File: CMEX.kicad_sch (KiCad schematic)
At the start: 0 parts

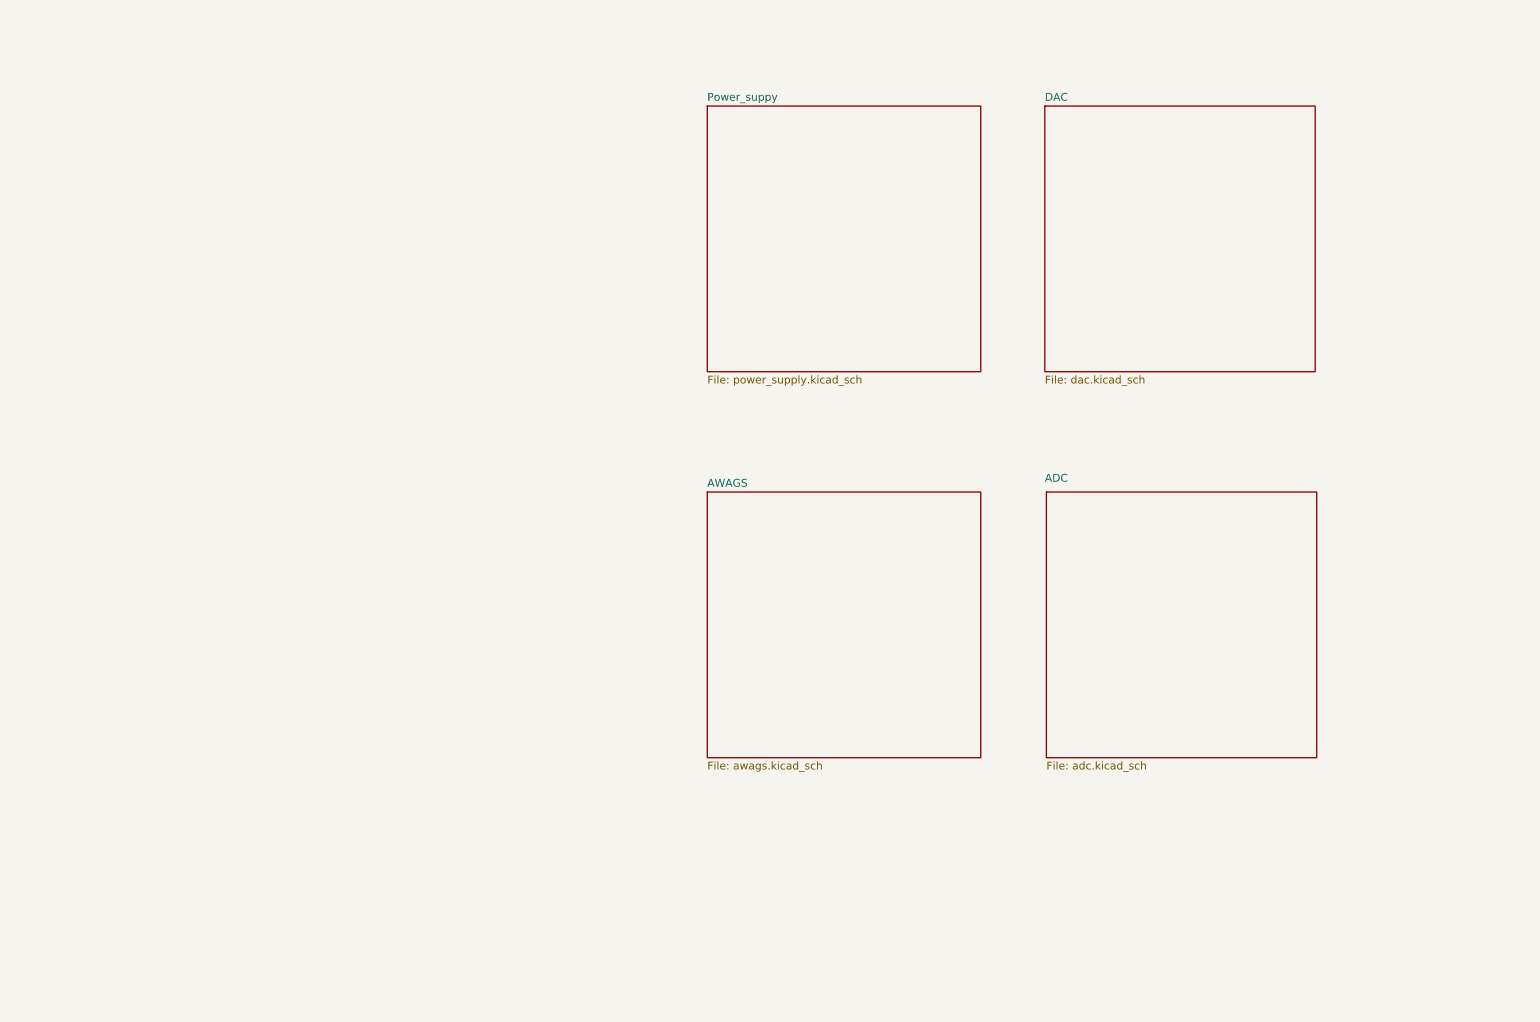
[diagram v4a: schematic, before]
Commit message: Changed global to hierarchichal lables, reorganized main sheet to get pins to connector.
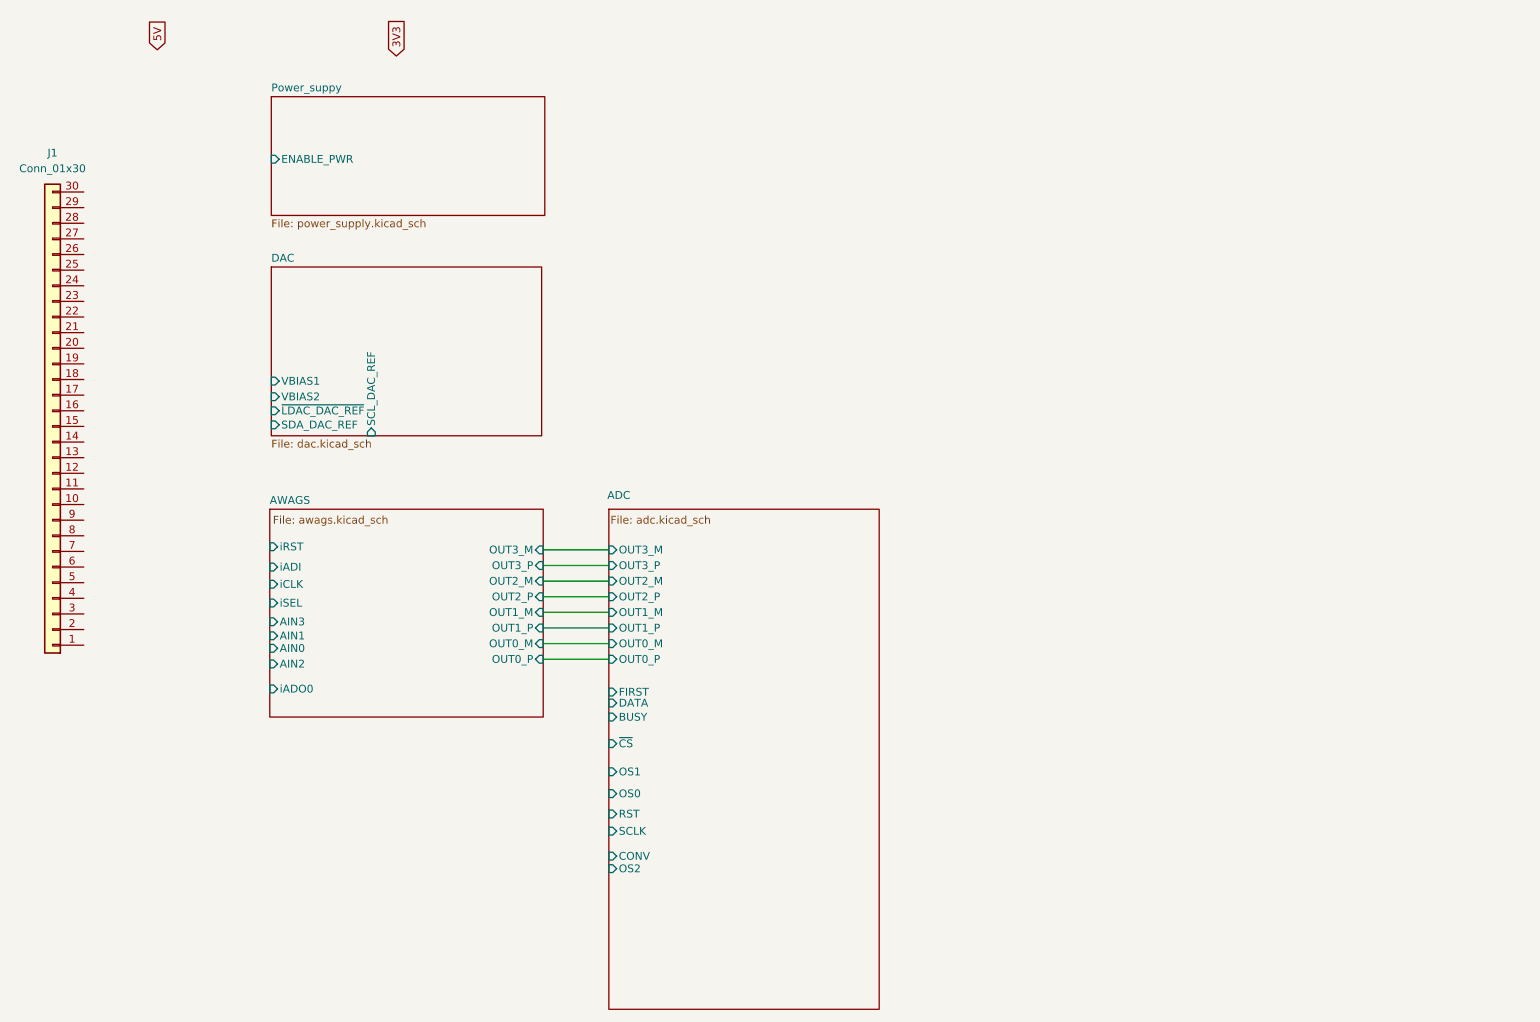
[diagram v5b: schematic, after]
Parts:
- added J1: Conn_01x30, symbol Connector_Generic:Conn_01x30
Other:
- sheet ADC ports: added BUSY, CONV, DATA, FIRST, OS0, OS1, OS2, OUT0_M, OUT0_P, OUT1_M, OUT1_P, OUT2_M, OUT2_P, OUT3_M, OUT3_P, RST, SCLK, ~{CS}; removed none
- sheet AWAGS ports: added AIN0, AIN1, AIN2, AIN3, OUT0_M, OUT0_P, OUT1_M, OUT1_P, OUT2_M, OUT2_P, OUT3_M, OUT3_P, iADI, iADO0, iCLK, iRST, iSEL; removed none
- sheet DAC ports: added SCL_DAC_REF, SDA_DAC_REF, VBIAS1, VBIAS2, ~{LDAC_DAC_REF}; removed none
- sheet Power_suppy ports: added ENABLE_PWR; removed none

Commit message: Added connector to all sheets.
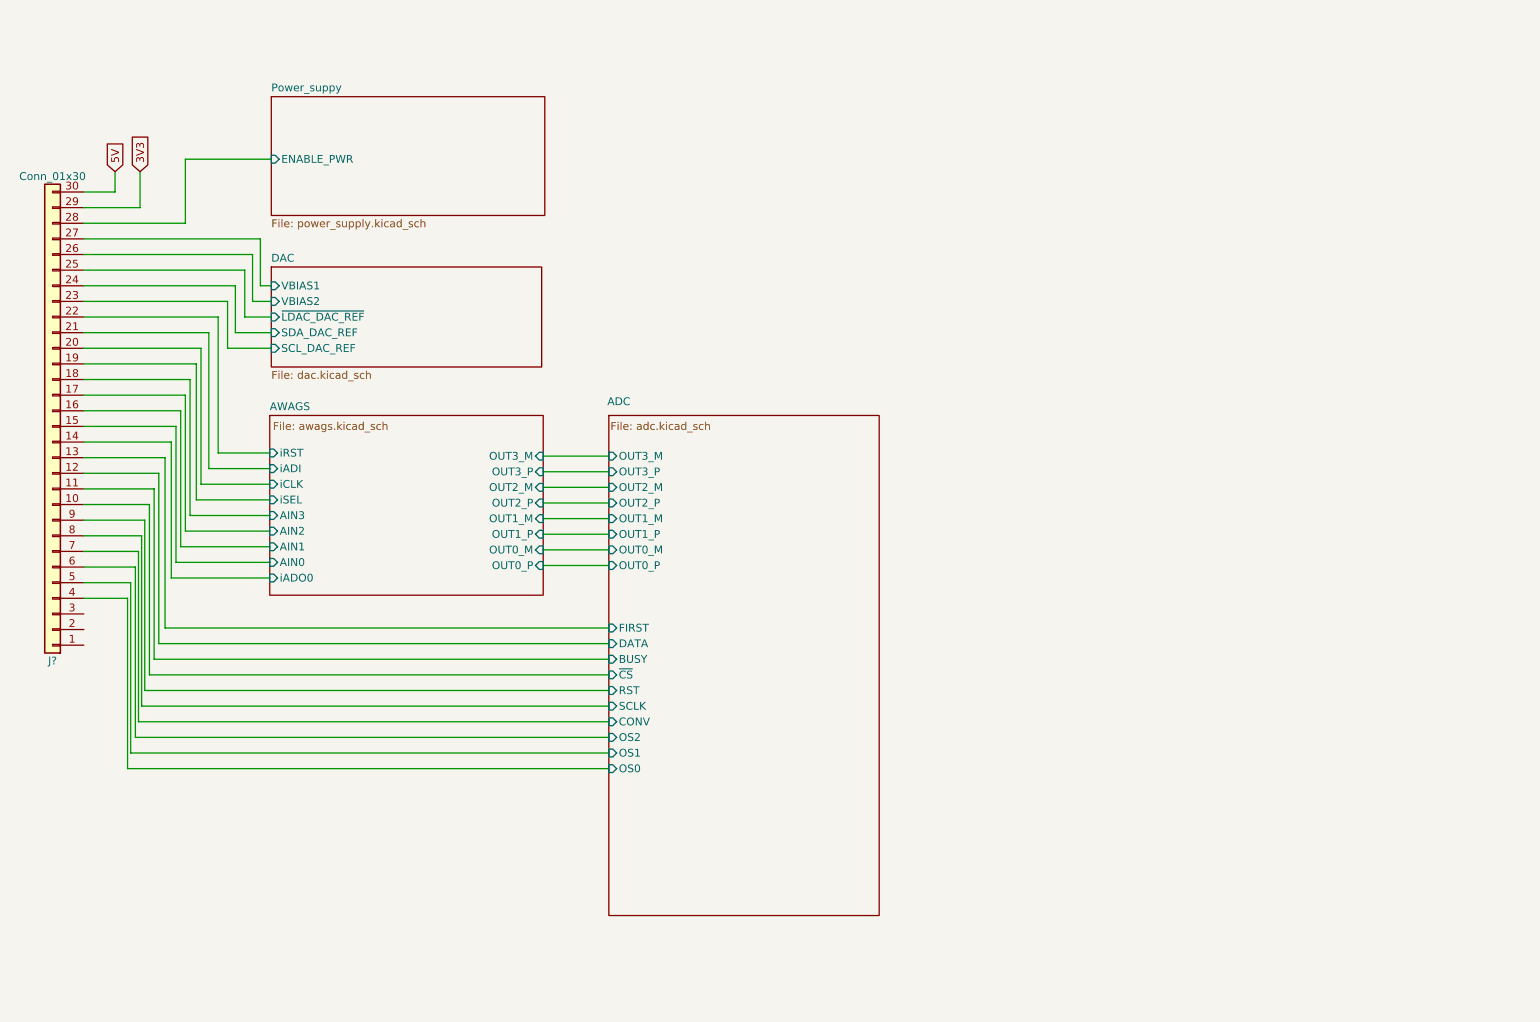
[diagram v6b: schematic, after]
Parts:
- J?: renamed from J1; footprint (none) -> Connector_PinHeader_1.27mm:PinHeader_1x30_P1.27mm_Vertical
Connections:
- net 3V3: now also J?.29 (Pin_29)
- net 5V: now also J?.30 (Pin_30)
- net ADC/BUSY: now also J?.11 (Pin_11)
- net ADC/CONV: now also J?.7 (Pin_7)
- net ADC/DATA: now also J?.12 (Pin_12)
- net ADC/FIRST: now also J?.13 (Pin_13)
- net ADC/OS0: now also J?.4 (Pin_4)
- net ADC/OS1: now also J?.5 (Pin_5)
- net ADC/OS2: now also J?.6 (Pin_6)
- net ADC/RST: now also J?.9 (Pin_9)
- net ADC/SCLK: now also J?.8 (Pin_8)
- net ADC/~{CS}: now also J?.10 (Pin_10)
- net AWAGS/AIN0: now also J?.15 (Pin_15)
- net AWAGS/AIN1: now also J?.16 (Pin_16)
- net AWAGS/AIN2: now also J?.17 (Pin_17)
- net AWAGS/AIN3: now also J?.18 (Pin_18)
- net AWAGS/iADI: now also J?.21 (Pin_21)
- net AWAGS/iADO0: now also J?.14 (Pin_14)
- net AWAGS/iCLK: now also J?.20 (Pin_20)
- net AWAGS/iRST: now also J?.22 (Pin_22)
- net AWAGS/iSEL: now also J?.19 (Pin_19)
- net DAC/SCL_DAC_REF: now also J?.23 (Pin_23)
- net DAC/SDA_DAC_REF: now also J?.24 (Pin_24)
- net DAC/VBIAS1: now also J?.27 (Pin_27)
- net DAC/VBIAS2: now also J?.26 (Pin_26)
- net DAC/~{LDAC_DAC_REF}: now also J?.25 (Pin_25)
- net Power_suppy/ENABLE_PWR: now also J?.28 (Pin_28)

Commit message: Schematic finished, ready for review.
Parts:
- J1: renamed from J?; footprint Connector_PinHeader_1.27mm:PinHeader_1x30_P1.27mm_Vertical -> (none)
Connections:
- net GND: now reaches J1.3 (Pin_3)
- no-connect marks 0 -> 2
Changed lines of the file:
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@@
 (kicad_sch (version 20230121) (generator eeschema)
   (paper "A4")
+  (junction (at 55.118 58.42) (diameter 0) (color 0 0 0 0)
+  )
+  (junction (at 48.768 131.572) (diameter 0) (color 0 0 0 0)
+  )
+  (junction (at 48.514 55.88) (diameter 0) (color 0 0 0 0)
+  )
+  (no_connect (at 45.974 129.54))
+  (no_connect (at 45.974 127))
   (wire (pts (xy 76.454 73.66) (xy 73.406 73.66))
     (stroke (width 0) (type default))
@@
     (stroke (width 0) (type default))
   )
-  (wire (pts (xy 45.974 55.88) (xy 51.054 55.88))
+  (wire (pts (xy 45.974 55.88) (xy 48.514 55.88))
     (stroke (width 0) (type default))
   )
@@
     (stroke (width 0) (type default))
   )
+  (wire (pts (xy 45.974 124.46) (xy 48.768 124.46))
+    (stroke (width 0) (type default))
+  )
   (wire (pts (xy 74.676 71.12) (xy 76.454 71.12))
     (stroke (width 0) (type default))
@@
     (stroke (width 0) (type default))
   )
+  (wire (pts (xy 48.768 124.46) (xy 48.768 131.572))
+    (stroke (width 0) (type default))
+  )
   (wire (pts (xy 120.65 101.346) (xy 131.318 101.346))
     (stroke (width 0) (type default))
@@
     (stroke (width 0) (type default))
   )
+  (wire (pts (xy 48.768 131.572) (xy 48.768 135.636))
+    (stroke (width 0) (type default))
+  )
   (wire (pts (xy 63.246 108.458) (xy 63.246 86.36))
     (stroke (width 0) (type default))
@@
   )
   (wire (pts (xy 45.974 68.58) (xy 72.136 68.58))
+    (stroke (width 0) (type default))
+  )
+  (wire (pts (xy 48.514 55.88) (xy 51.054 55.88))
     (stroke (width 0) (type default))
   )
@@
     )
   )
+  (symbol (lib_id "power:GND") (at 48.768 135.636 0) (unit 1)
+    (in_bom yes) (on_board yes) (dnp no) (fields_autoplaced)
+    (property "Reference" "#PWR01" (at 48.768 141.986 0)
+      (effects (font (size 1.27 1.27)) hide)
+    )
+    (property "Value" "GND" (at 48.768 139.446 0)
+      (effects (font (size 1.27 1.27)))
+    )
+    (property "Footprint" "" (at 48.768 135.636 0)
+      (effects (font (size 1.27 1.27)) hide)
+    )
+    (property "Datasheet" "" (at 48.768 135.636 0)
+      (effects (font (size 1.27 1.27)) hide)
+    )
+    (pin "1")
+    (instances
+      (project "CMEX"
+        (path "/03c4a148-37f4-4d5a-ada3-efb0d725ba7b"
+          (reference "#PWR01") (unit 1)
+        )
+      )
+    )
+  )
+  (symbol (lib_id "power:PWR_FLAG") (at 55.118 58.42 270) (unit 1)
+    (in_bom yes) (on_board yes) (dnp no)
+    (property "Reference" "#FLG03" (at 57.023 58.42 0)
+      (effects (font (size 1.27 1.27)) hide)
+    )
+    (property "Value" "PWR_FLAG" (at 58.928 58.42 0)
+      (effects (font (size 1.27 1.27)))
+    )
+    (property "Footprint" "" (at 55.118 58.42 0)
+      (effects (font (size 1.27 1.27)) hide)
+    )
+    (property "Datasheet" "~" (at 55.118 58.42 0)
+      (effects (font (size 1.27 1.27)) hide)
+    )
+    (pin "1")
+    (instances
+      (project "CMEX"
+        (path "/03c4a148-37f4-4d5a-ada3-efb0d725ba7b"
+          (reference "#FLG03") (unit 1)
+        )
+      )
+    )
+  )
+  (symbol (lib_id "power:PWR_FLAG") (at 48.514 55.88 0) (unit 1)
+    (in_bom yes) (on_board yes) (dnp no)
+    (property "Reference" "#FLG01" (at 48.514 53.975 0)
+      (effects (font (size 1.27 1.27)) hide)
+    )
+    (property "Value" "PWR_FLAG" (at 48.514 52.07 0)
+      (effects (font (size 1.27 1.27)))
+    )
+    (property "Footprint" "" (at 48.514 55.88 0)
+      (effects (font (size 1.27 1.27)) hide)
+    )
+    (property "Datasheet" "~" (at 48.514 55.88 0)
+      (effects (font (size 1.27 1.27)) hide)
+    )
+    (pin "1")
+    (instances
+      (project "CMEX"
+        (path "/03c4a148-37f4-4d5a-ada3-efb0d725ba7b"
+          (reference "#FLG01") (unit 1)
+        )
+      )
+    )
+  )
   (symbol (lib_id "Connector_Generic:Conn_01x30") (at 40.894 93.98 180) (unit 1)
     (in_bom yes) (on_board yes) (dnp no) (fields_autoplaced)
-    (property "Reference" "J?" (at 40.894 132.08 0)
+    (property "Reference" "J1" (at 40.894 132.08 0)
       (effects (font (size 1.27 1.27)))
     )
@@
       (effects (font (size 1.27 1.27)))
     )
-    (property "Footprint" "Connector_PinHeader_1.27mm:PinHeader_1x30_P1.27mm_Vertical" (at 40.894 93.98 0)
+    (property "Footprint" "" (at 40.894 93.98 0)
       (effects (font (size 1.27 1.27)) hide)
     )
@@
       (project "CMEX"
         (path "/03c4a148-37f4-4d5a-ada3-efb0d725ba7b"
-          (reference "J?") (unit 1)
+          (reference "J1") (unit 1)
         )
       )
+    )
+  )
+  (symbol (lib_id "power:PWR_FLAG") (at 48.768 131.572 270) (unit 1)
+    (in_bom yes) (on_board yes) (dnp no)
+    (property "Reference" "#FLG02" (at 50.673 131.572 0)
+      (effects (font (size 1.27 1.27)) hide)
+    )
+    (property "Value" "PWR_FLAG" (at 52.578 131.572 0)
+      (effects (font (size 1.27 1.27)))
+    )
+    (property "Footprint" "" (at 48.768 131.572 0)
+      (effects (font (size 1.27 1.27)) hide)
+    )
+    (property "Datasheet" "~" (at 48.768 131.572 0)
+      (effects (font (size 1.27 1.27)) hide)
+    )
+    (pin "1")
+    (instances
+      (project "CMEX"
+        (path "/03c4a148-37f4-4d5a-ada3-efb0d725ba7b"
+          (reference "#FLG02") (unit 1)
+        )
+      )

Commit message: Layout erster Entwurf fertig.
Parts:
- J1: footprint (none) -> Connector_PinHeader_1.27mm:PinHeader_1x30_P1.27mm_Vertical
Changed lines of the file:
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@@
       (effects (font (size 1.27 1.27)))
     )
-    (property "Footprint" "" (at 40.894 93.98 0)
+    (property "Footprint" "Connector_PinHeader_1.27mm:PinHeader_1x30_P1.27mm_Vertical" (at 40.894 93.98 0)
       (effects (font (size 1.27 1.27)) hide)
     )
